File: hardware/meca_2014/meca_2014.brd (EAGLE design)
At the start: 100 x 80 mm, 128 parts, among them IC1 MAX3232CSE, IC10 74LVC1T45DBV, IC11 74LVC1T45DBV, IC12 LM2596S-ADJ, IC2 XMEGA128-A1, IC3 LM1086CS-3.3, IC4 MPXV5100GC6U, IC5 LM2596S-ADJ, IC6 74LVC4245APW, IC8 MPXV5100GC6U, T1 NTR4503NT1G, T2 NTR4503NT1G

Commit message: meca 2014 : routing done
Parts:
- moved IC12 401.9 mm to (90.8, 53.3), turned to 270 degrees
- moved IC5 376.7 mm to (90.8, 32.4), turned to 270 degrees
- moved R30 359.9 mm to (82.5, 62.2), flipped to the bottom, turned to 90 degrees
- moved R28 359.1 mm to (83.8, 66.0), flipped to the bottom
- moved R29 348.7 mm to (78.7, 66.0), flipped to the bottom
- moved T2 346.9 mm to (78.7, 62.2), flipped to the bottom, turned to 270 degrees
- moved D4 339.8 mm to (74.3, 64.1), flipped to the bottom, turned to 270 degrees
- moved VPMP1 339.6 mm to (74.9, 74.9), turned to 180 degrees
- moved IC6 330.5 mm to (17.8, 12.7)
- moved VPMP0 325.1 mm to (66.7, 74.9), turned to 180 degrees
- moved ARM_MOT 323.6 mm to (62.9, 5.71)
- moved R32 321.7 mm to (43.9, 22.4)
- moved R31 320.9 mm to (47.5, 22.5), turned to 180 degrees
- moved T1 310.3 mm to (64.8, 61.6), flipped to the bottom, turned to 90 degrees
- moved R26 306.1 mm to (64.8, 65.4), flipped to the bottom, turned to 180 degrees
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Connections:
- removed net PWM1: SV7.3
- removed net PWM2: SV6.3
- removed net PWM3: SV1.3
- removed net PWM3_3V3: IC6.18
- removed net VCCA: IC11.1
- removed net VCCB: IC11.6
- net +3V3: now also IC11.1
- net +5V: now also IC11.6
- net PWM1_5V: now also SV7.3
- net PWM2_5V: now also SV6.3
- net PWM3_5V: now also SV1.3
- net PWM_C4_3V3: now also IC6.18; no longer IC6.20
- net PWM_D1_3V3: now also IC6.20; no longer IC6.19
- net PWM_D2_3V3: now also IC6.19
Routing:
- net +3V3: track 0.00 -> 417.6 mm, vias 0 -> 7
- net +5V: track 0.00 -> 354.5 mm, vias 0 -> 8
- net GND: track 0.00 -> 249.4 mm, vias 0 -> 70
- net PW: track 0.00 -> 162.1 mm, vias 0 -> 4
- net VACUUM_PUMP_1_VOLTAGE_MONITOR_0-1V: track 0.00 -> 143.6 mm, vias 0 -> 1
- net VACUUM_PUMP_0_VOLTAGE_MONITOR_0-1V: track 0.00 -> 122.1 mm, vias 0 -> 1
- net AX12_5V: track 0.00 -> 93.2 mm, vias 0 -> 3
- net +10V: track 0.00 -> 92.4 mm, vias 0 -> 1
- net TX_232: track 0.00 -> 83.2 mm, vias 0 -> 4
- net VACCUM_PRESSURE_0_0-1V: track 0.00 -> 80.4 mm, vias 0 -> 1
- net RX_232: track 0.00 -> 77.0 mm, vias 0 -> 4
- net VACCUM_PRESSURE_1_0-1V: track 0.00 -> 74.1 mm, vias 0 -> 1
- net VACUUM_PUMP_1_CMD_3V3: track 0.00 -> 72.6 mm, vias 0 -> 5
- net /RESET_3V3: track 0.00 -> 61.2 mm, vias 0 -> 2
- net VACUUM_PUMP_0_CMD_3V3: track 0.00 -> 58.1 mm, vias 0 -> 5
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- added copper zone on layer 1, net GND
- added copper zone on layer 16, net GND

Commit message: MECA 2014 : fixes to brd
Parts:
- moved C36 53.3 mm to (2.41, 10.3)
- moved C7 11.5 mm to (32.3, 16.9), turned to 270 degrees
- moved C18 8.52 mm to (13.3, 34.9), turned to 270 degrees
- moved R15 8.05 mm to (33.5, 52.6), turned to 180 degrees
- moved C17 7.14 mm to (13.2, 42.8), turned to 90 degrees
- moved C16 6.14 mm to (20.6, 30.7)
- moved C40 4.85 mm to (88.5, 42.7), turned to 180 degrees
- moved D4 4.49 mm to (77.3, 67.4), turned to 180 degrees
- moved C14 4.12 mm to (34.8, 45.0), turned to 90 degrees
- moved PW_BAT 3.69 mm to (86.9, 75.1)
- moved D5 3.53 mm to (67.4, 67.2), turned to 180 degrees
- moved R28 3.47 mm to (82.2, 63.0)
- moved R29 3.26 mm to (77.6, 63.0)
- moved VPMP1 2.54 mm to (77.5, 75.1)
- moved R30 2.25 mm to (81.9, 60.1)
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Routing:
- net VACUUM_PUMP_1_VOLTAGE_MONITOR_0-1V: track 143.6 -> 163.3 mm
- net GND: track 249.4 -> 237.8 mm, vias 70 -> 84
- net +5V: track 354.5 -> 345.3 mm
- net PW: track 162.1 -> 169.4 mm
- net +3V3: track 417.6 -> 410.6 mm
- net /RESET_3V3: track 61.2 -> 54.3 mm
- net N$14: track 10.8 -> 15.6 mm
- net N$17: track 37.8 -> 33.8 mm, vias 2 -> 0
- net VACUUM_PUMP_1_CMD_3V3: track 72.6 -> 69.1 mm
- net N$46: track 9.04 -> 12.5 mm
- net VACUUM_PUMP_0: track 12.9 -> 10.7 mm
- net N$45: track 19.3 -> 20.7 mm
- net VACUUM_PUMP_0_VOLTAGE_MONITOR_0-1V: track 122.1 -> 123.1 mm
- net +10V: track 92.4 -> 93.3 mm
- net VACUUM_PUMP_1: track 12.2 -> 11.6 mm

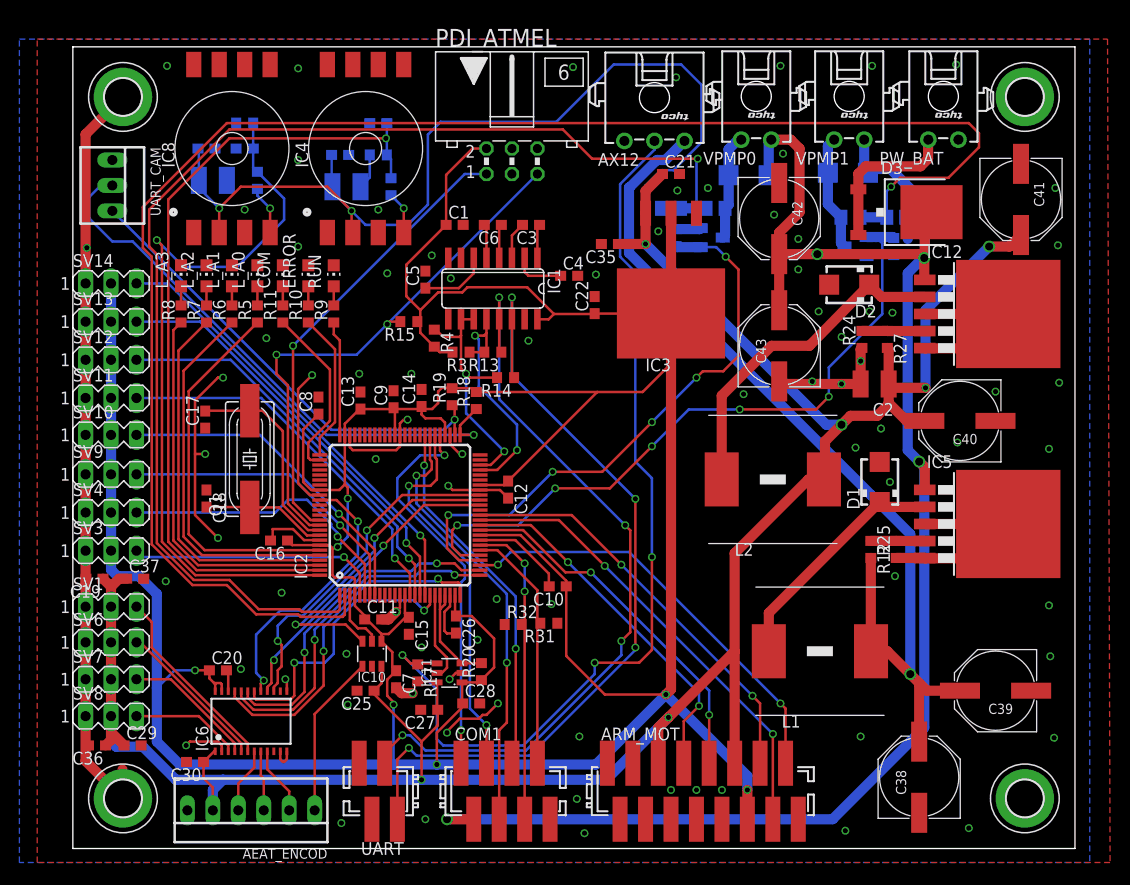
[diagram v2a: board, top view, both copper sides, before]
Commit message: power supply rerouted, board ready to be sent to manufacturer
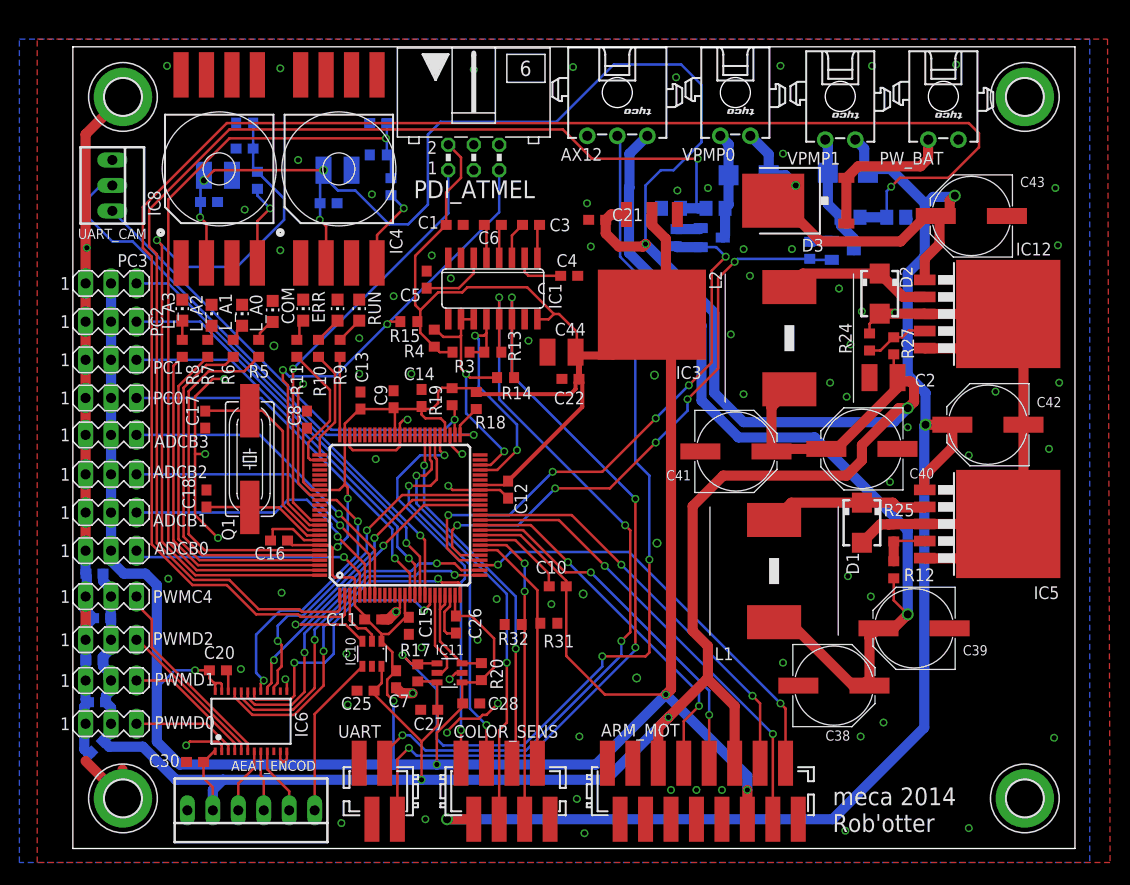
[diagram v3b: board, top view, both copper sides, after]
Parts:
- removed ERROR: LED_G, robotter_diode:CHIP-LED0805
- removed SV1, SV6, SV7, SV8: (no value), con-lstb:MA03-1
- added C44: 10µF 25V, robotter_capacitor:C1210
- added ERR: LED_G, robotter_diode:CHIP-LED0805
- added PWMC4, PWMD0, PWMD1, PWMD2: (no value), con-lstb:MA03-1
- moved C35 62.9 mm to (2.92, 23.0), flipped to the bottom, turned to 0 degrees
- moved C41 38.0 mm to (66.2, 39.6), turned to 0 degrees
- moved C42 29.3 mm to (91.3, 42.3), turned to 180 degrees
- moved C43 23.1 mm to (89.7, 63.1), turned to 180 degrees
- moved L2 14.2 mm to (71.5, 50.9), turned to 270 degrees
- moved C38 12.5 mm to (75.9, 16.3), turned to 0 degrees
- moved D3 10.9 mm to (72.4, 64.6), turned to 90 degrees
- moved C39 10.2 mm to (83.9, 22.0)
- moved C40 10.2 mm to (78.7, 39.9)
- moved L1 9.22 mm to (70.0, 27.7), turned to 270 degrees
- moved C21 8.67 mm to (52.3, 62.7), turned to 180 degrees
- moved R30 8.39 mm to (73.5, 59.7), turned to 270 degrees
- moved C19 8.13 mm to (2.16, 18.8), flipped to the bottom, turned to 0 degrees
- moved C22 7.75 mm to (49.7, 46.9), turned to 180 degrees
- moved C32 5.34 mm to (13.6, 64.5)
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- renumbered COM1 to COLOR_SENS, SV10 to ADCB3, SV11 to PC0, SV12 to PC1, SV13 to PC2, SV14 to PC3, SV3 to ADCB0, SV4 to ADCB1, SV9 to ADCB2
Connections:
- net ADC0 renamed ADCB0
- net ADC1 renamed ADCB1
- net ADC2 renamed ADCB2
- net ADC3 renamed ADCB3
- net PC0 renamed PC0_3V3
- net PC1 renamed PC1_3V3
- net PC2 renamed PC2_3V3
- net PC3 renamed PC3_3V3
- removed net PWM0_5V: IC6.3, SV8.3
- removed net PWM1_5V: IC6.4, SV7.3
- removed net PWM2_5V: IC6.5, SV6.3
- removed net PWM3_5V: IC6.6, SV1.3
- new net PWM_C4_5V: IC6.6, PWMC4.3
- new net PWM_D0_5V: IC6.3, PWMD0.3
- new net PWM_D1_5V: IC6.4, PWMD1.3
- new net PWM_D2_5V: IC6.5, PWMD2.3
- net +3V3: now also C44.1
- net +5V: now also PWMC4.2, PWMD0.2, PWMD1.2, PWMD2.2; no longer SV1.2, SV6.2, SV7.2, SV8.2
- net GND: now also C44.2, ERR.C, PWMC4.1, PWMD0.1, PWMD1.1, PWMD2.1; no longer ERROR.C, SV1.1, SV6.1, SV7.1, SV8.1
- net N$4: now also ERR.A; no longer ERROR.A
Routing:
- net GND: track 237.8 -> 265.1 mm, vias 84 -> 89
- net PWM_C4_5V: track 0.00 -> 20.0 mm
- net PWM3_5V: track 19.0 -> 0.00 mm
- net N$17: track 33.8 -> 15.0 mm
- net PWM_D2_5V: track 0.00 -> 15.5 mm
- net PWM2_5V: track 15.4 -> 0.00 mm
- net PWM1_5V: track 13.3 -> 0.00 mm
- net PWM_D1_5V: track 0.00 -> 13.2 mm
- net PWM0_5V: track 10.9 -> 0.00 mm
- net PWM_D0_5V: track 0.00 -> 10.6 mm
- net +5V: track 345.3 -> 355.4 mm
- net VACUUM_PUMP_1_CMD_3V3: track 69.1 -> 59.9 mm
- net N$16: track 24.2 -> 16.0 mm
- net N$15: track 4.25 -> 8.38 mm
- net N$12: track 17.6 -> 13.6 mm
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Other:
- board text added: "meca 2014 Rob'otter"

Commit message: few changes before fabrication
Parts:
- added C45, C46: 10µF 25V, robotter_capacitor:C1210
- moved R30 4.95 mm to (68.6, 59.7)
- moved T2 4.19 mm to (72.6, 59.6)
- moved R29 3.09 mm to (77.1, 59.9)
- moved R28 2.33 mm to (81.3, 60.8)
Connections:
- net GND: now also C45.2, C46.2
- net VACUUM_PUMP_0_VOLTAGE_MONITOR_0-1V: now also C46.1
- net VACUUM_PUMP_1_VOLTAGE_MONITOR_0-1V: now also C45.1
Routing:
- net VACUUM_PUMP_1_CMD_3V3: track 59.9 -> 55.9 mm
- net VACUUM_PUMP_1_VOLTAGE_MONITOR_0-1V: track 163.3 -> 166.7 mm
- net GND: track 265.1 -> 262.6 mm, vias 89 -> 97
- net VACUUM_PUMP_1: track 12.2 -> 14.5 mm
- net +5V: track 355.4 -> 357.5 mm

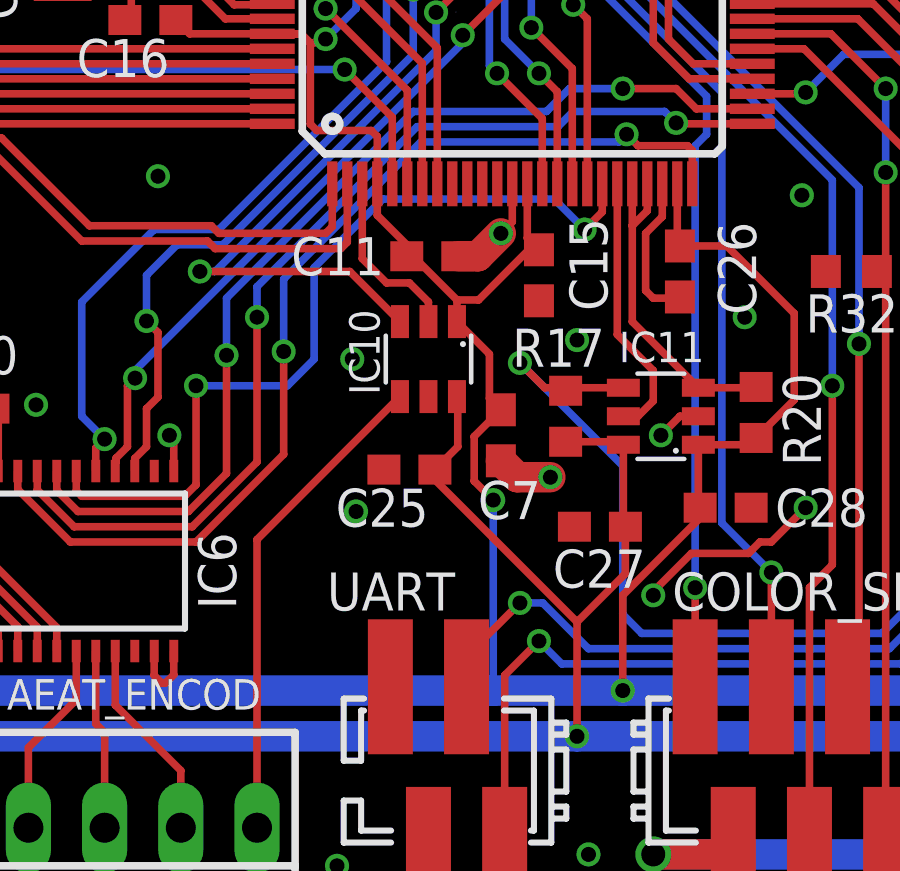
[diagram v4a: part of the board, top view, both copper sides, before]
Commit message: mouser component ref added
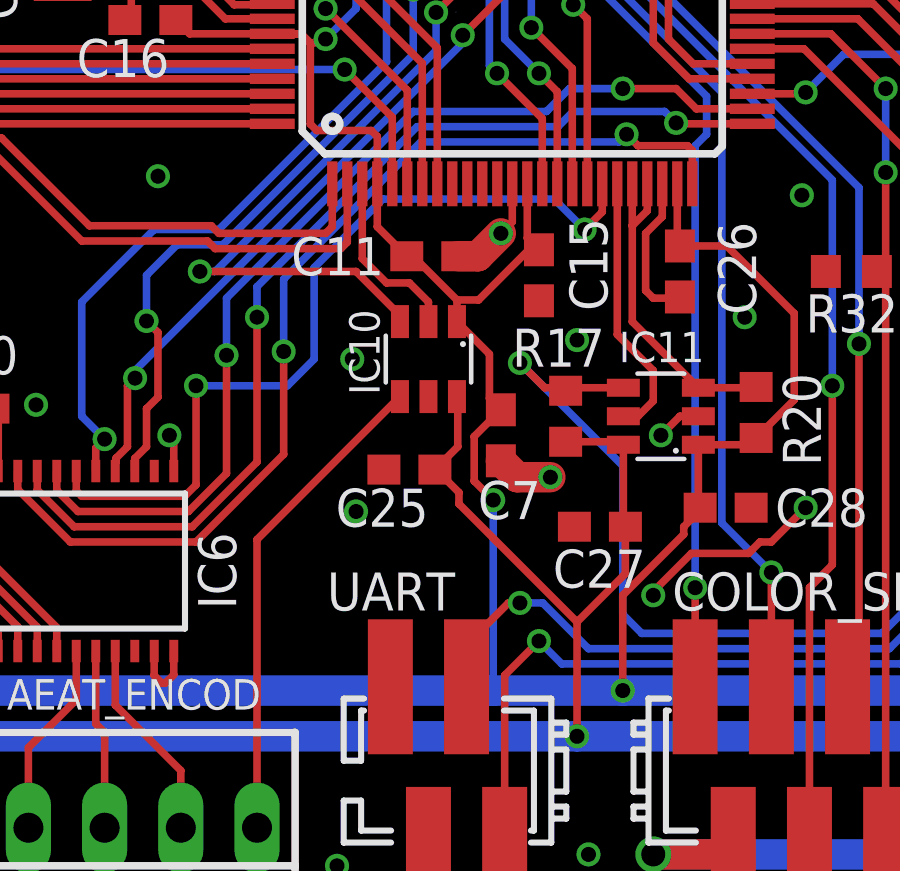
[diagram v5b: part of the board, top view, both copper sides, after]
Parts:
- AEAT_ENCOD: device con-molex:22-23-2061 -> robotter_connector:22-23-2061
- AX12: device con-amp:1445055-3 -> robotter_connector:1445055-3
- PW_BAT: device con-amp:1445055-2 -> robotter_connector:1445055-2
- UART_CAM: device con-molex:22-23-2031 -> robotter_connector:22-23-2031
